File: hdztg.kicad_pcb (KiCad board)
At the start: 4 copper layers, 25 x 18 mm, 8 parts, among them J1 20374-R20E-31, Q1 2N7002KDW 72K

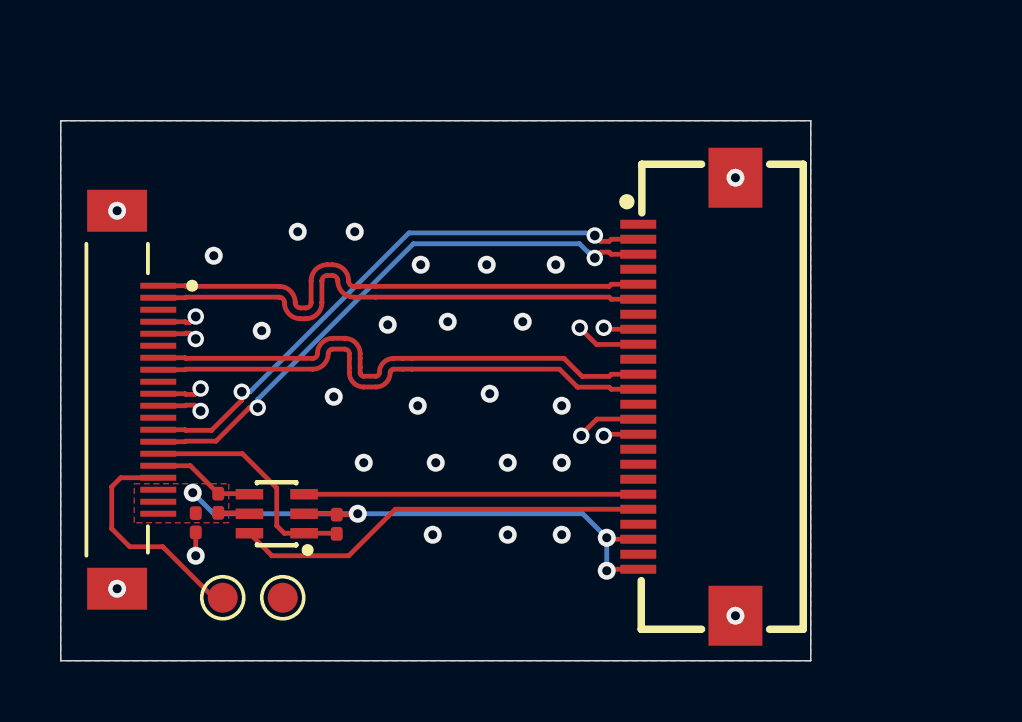
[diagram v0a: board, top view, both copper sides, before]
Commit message: update pcb, fix level shifter
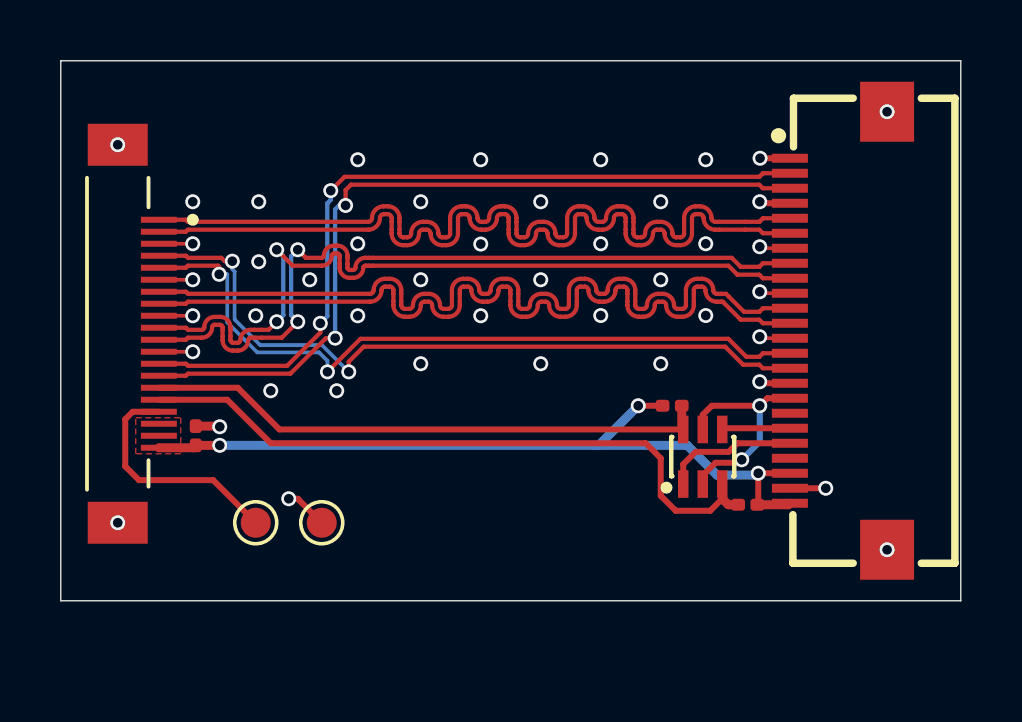
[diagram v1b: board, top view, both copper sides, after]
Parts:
- moved R2 17.7 mm to (122.9, 90.8), turned to 0 degrees
- moved Q1 14.3 mm to (121.4, 89.2), turned to 0 degrees
- moved R1 11.9 mm to (120.4, 87.5), turned to 0 degrees
- moved FPC1 5.51 mm to (125.9, 85.0)
- moved C1 2.90 mm to (104.5, 88.5), turned to 90 degrees
- moved TP2 2.82 mm to (108.7, 91.4)
- moved TP1 2.73 mm to (106.5, 91.4)
- moved J1 2.20 mm to (101.9, 85.1)
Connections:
- FPC1 pad 17: unconnected-(FPC1-Pad17) -> +1V8
- Q1 pad 1: /SCL_3V3 -> /SCL_1V8
- Q1 pad 2: +3V3 -> +1V8
- Q1 pad 3: /SDA_1V8 -> /SDA_3V3
- Q1 pad 4: /SDA_3V3 -> /SDA_1V8
- Q1 pad 5: +3V3 -> +1V8
- Q1 pad 6: /SCL_1V8 -> /SCL_3V3
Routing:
- net /SDA_3V3: track 3.43 -> 22.3 mm
- net GND: track 0.68 -> 14.2 mm, vias 26 -> 45
- net /MIPI_D2+: track 17.9 -> 29.2 mm
- net /MIPI_D2-: track 17.9 -> 29.2 mm
- net /MIPI_D0-: track 17.9 -> 29.1 mm
- net /MIPI_D0+: track 17.9 -> 29.1 mm
- net /SCL_3V3: track 7.79 -> 18.8 mm
- net /SCL_1V8: track 13.9 -> 4.50 mm
- net /SDA_1V8: track 11.1 -> 2.27 mm
- net /MIPI_CK-: track 18.0 -> 26.3 mm
- net /MIPI_CK+: track 18.4 -> 26.3 mm
- net +1V8: track 0.00 -> 7.47 mm, vias 0 -> 2
- net /MIPI_D1+: track 19.2 -> 26.5 mm
- net /MIPI_D1-: track 19.0 -> 26.3 mm
- net /MIPI_D3-: track 17.8 -> 24.7 mm
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- removed copper zone on B.Cu, net GND
- removed copper zone on F.Cu, net GND
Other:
- board size 25 x 18 mm -> 30 x 18 mm

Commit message: update pcb
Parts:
- moved C1 50.3 mm to (154.8, 87.9), turned to 0 degrees
- moved TP1 45.7 mm to (152.1, 88.6)
- moved TP2 43.4 mm to (152.1, 91.6)
- moved R1 34.5 mm to (154.8, 89.7)
- moved R2 31.9 mm to (154.8, 91.4)
- moved Q1 15.8 mm to (105.8, 91.5)
- moved FPC1 4.86 mm to (130.8, 85.3)
- moved J1 1.38 mm to (102.7, 84.0), turned to 90 degrees
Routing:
- net +3V3: track 26.5 -> 0.00 mm, vias 3 -> 0
- net /SDA_3V3: track 22.3 -> 0.00 mm
- net /SCL_3V3: track 18.8 -> 0.00 mm
- net /MIPI_D3+: track 24.6 -> 37.7 mm, vias 2 -> 0
- net /MIPI_D3-: track 24.7 -> 37.7 mm, vias 2 -> 0
- net /MIPI_CK-: track 26.3 -> 37.7 mm, vias 2 -> 0
- net /MIPI_CK+: track 26.3 -> 37.7 mm, vias 2 -> 0
- net /MIPI_D1-: track 26.3 -> 34.6 mm
- net /MIPI_D1+: track 26.5 -> 34.8 mm
- net /PROG: track 7.92 -> 0.00 mm
- net +1V8: track 7.47 -> 0.00 mm, vias 2 -> 0
- net /MIPI_D0-: track 29.1 -> 35.0 mm, vias 0 -> 2
- net /MIPI_D0+: track 29.1 -> 34.5 mm, vias 0 -> 2
- net /MIPI_D2+: track 29.2 -> 34.5 mm, vias 0 -> 2
- net /MIPI_D2-: track 29.2 -> 34.2 mm, vias 0 -> 2
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- added copper zone on B.Cu, net GND
- added copper zone on F.Cu, net GND
- removed copper zone on F.Cu, net +3V3
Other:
- board size 30 x 18 mm -> 35 x 18 mm

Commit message: update pcb
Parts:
- moved C1 55.4 mm to (99.9, 80.6), turned to 90 degrees
- moved TP1 46.4 mm to (107.0, 77.8)
- moved TP2 45.3 mm to (109.0, 77.8)
- moved R1 29.8 mm to (125.0, 90.6), turned to 180 degrees
- moved R2 27.2 mm to (127.6, 91.4)
- moved Q1 21.5 mm to (127.1, 89.2)
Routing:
- net /SDA_3V3: track 0.00 -> 39.0 mm
- net /SCL_3V3: track 0.00 -> 35.7 mm
- net /PROG: track 0.00 -> 7.75 mm
- net +1V8: track 0.00 -> 7.29 mm, vias 0 -> 2
- net /SCL_1V8: track 0.00 -> 3.53 mm
- net +3V3: track 0.00 -> 2.82 mm, vias 0 -> 5
- net /SDA_1V8: track 0.00 -> 1.51 mm
- net GND: track 9.90 -> 10.5 mm, vias 55 -> 68
- added copper zone on F.Cu, net +3V3
- added copper zone on In2.Cu, net +3V3
- removed copper zone on In2.Cu, net GND
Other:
- board size 35 x 18 mm -> 37 x 18 mm

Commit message: prod
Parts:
- removed FPC1: FPC-05FB-24PH20, EasyEDA:FPC-SMD_24P-P0.50_FPC-05FB-24PH20
- removed Q1: 2N7002KDW 72K, EasyEDA:SOT-363_L2.1-W1.3-P0.65-LS2.3-BL
- removed TP1, TP2: TestPoint, TestPoint:TestPoint_Pad_D1.0mm
- added J2: FPC-05FB-24PH20, EasyEDA:FPC-SMD_24P-P0.50_FPC-05FB-24PH20, F.Cu at (111.0, 70.0)
- added Q2: BSS138DW-7-F, EasyEDA:SC-70-6_L2.2-W1.3-P0.65-LS2.1-TL, F.Cu at (105.8, 64.7)
- moved R2 36.6 mm to (102.8, 64.5)
- moved R1 33.2 mm to (102.8, 66.0), turned to 0 degrees
- moved J1 24.9 mm to (82.0, 70.0), turned to -90 degrees
- moved C1 16.7 mm to (85.1, 72.8)
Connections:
- R1 pad 1: +3V3 -> /SCL_3V3
- R1 pad 2: /SCL_3V3 -> +3V3
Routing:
- net /PROG: track 7.75 -> 0.00 mm
- net /SDA_3V3: track 39.0 -> 32.5 mm
- net /MIPI_D3+: track 37.7 -> 33.2 mm
- net /MIPI_D3-: track 37.7 -> 33.2 mm
- net /MIPI_CK-: track 37.7 -> 33.2 mm
- net /MIPI_CK+: track 37.7 -> 33.2 mm
- net /SCL_1V8: track 3.53 -> 6.64 mm
- net /MIPI_D1-: track 34.8 -> 31.8 mm
- net /MIPI_D1+: track 34.8 -> 31.9 mm
- net /MIPI_D0-: track 34.9 -> 32.0 mm
- net /MIPI_D0+: track 34.9 -> 32.0 mm
- net /SCL_3V3: track 35.7 -> 33.0 mm, vias 0 -> 2
- net /MIPI_D2+: track 34.5 -> 31.8 mm
- net /MIPI_D2-: track 34.5 -> 31.8 mm
- net /SDA_1V8: track 1.51 -> 3.26 mm
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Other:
- board size 37 x 18 mm -> 35 x 20 mm

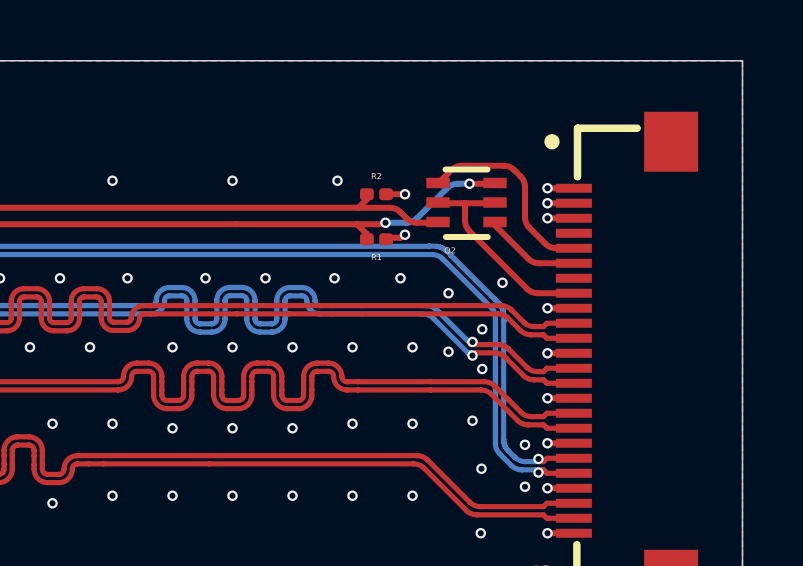
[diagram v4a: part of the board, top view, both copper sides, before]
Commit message: fix bottom reference stitching
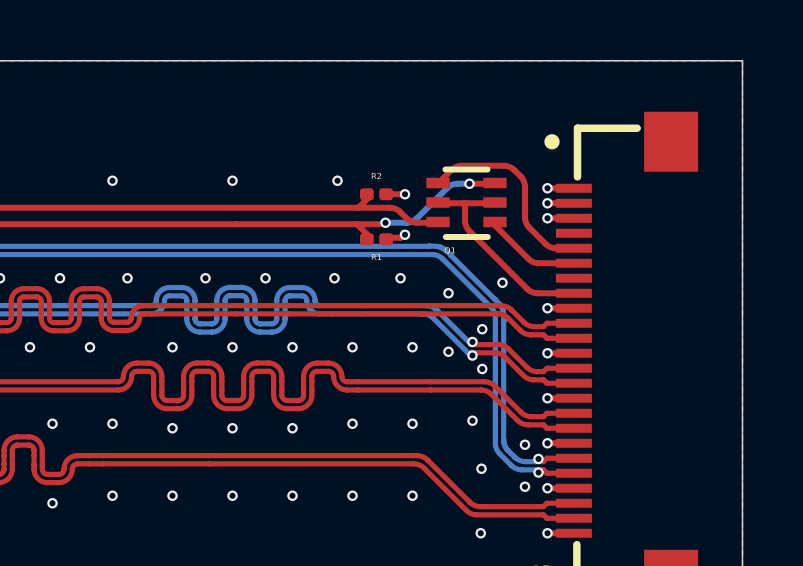
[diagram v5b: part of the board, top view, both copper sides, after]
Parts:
- renumbered Q2 to Q1
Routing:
- added copper zone on In2.Cu, net GND

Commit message: manufacturable version (pcb way)
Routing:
- net GND: vias 68 -> 65

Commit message: jlcpcb rev. 1
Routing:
- net GND: vias 65 -> 55

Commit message: jlcpcb production
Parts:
- C1: footprint Capacitor_SMD:C_0201_0603Metric -> Capacitor_SMD:C_0402_1005Metric
- R1, R2: footprint Resistor_SMD:R_0201_0603Metric -> Resistor_SMD:R_0402_1005Metric
- moved R1 4.44 mm to (101.0, 61.9), turned to 180 degrees
- moved Q1 2.34 mm to (104.0, 63.2)
- moved R2 2.27 mm to (101.0, 63.1)
- moved C1 1.17 mm to (85.3, 74.0), turned to -90 degrees
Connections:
- R2 pad 1: /SDA_3V3 -> +3V3
- R2 pad 2: +3V3 -> /SDA_3V3
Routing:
- net /SCL_1V8: track 6.64 -> 9.84 mm
- net /SDA_1V8: track 3.26 -> 6.27 mm
- net +1V8: track 7.10 -> 9.57 mm
- net GND: track 10.2 -> 12.6 mm, vias 55 -> 58
- net /SDA_3V3: track 32.5 -> 31.1 mm
- net +3V3: track 3.10 -> 4.46 mm, vias 6 -> 4
- net /SCL_3V3: track 33.0 -> 34.3 mm, vias 2 -> 3
- net /MIPI_D2-: track 31.8 -> 32.4 mm
- net /MIPI_D0-: track 31.9 -> 32.5 mm
- net /MIPI_D0+: track 31.9 -> 32.5 mm
- net /MIPI_D2+: track 31.7 -> 32.2 mm
- net /MIPI_D1+: track 31.8 -> 32.3 mm
